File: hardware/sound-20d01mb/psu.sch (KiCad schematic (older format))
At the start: 26 parts

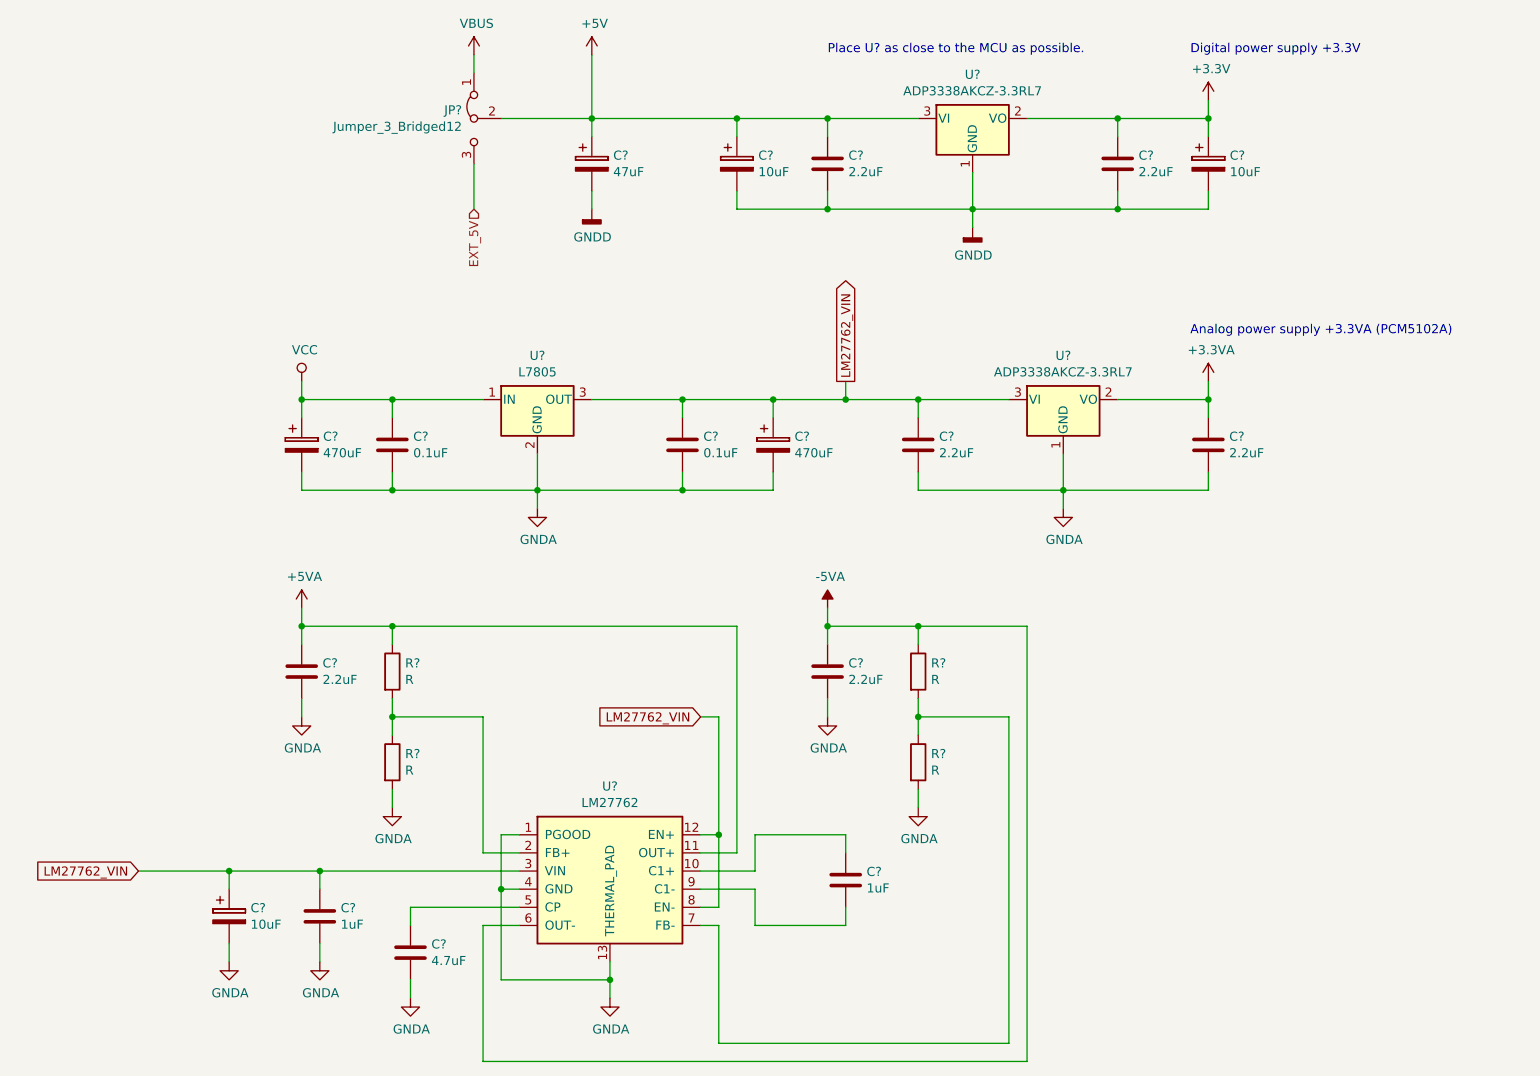
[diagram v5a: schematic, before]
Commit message: Added AD1938
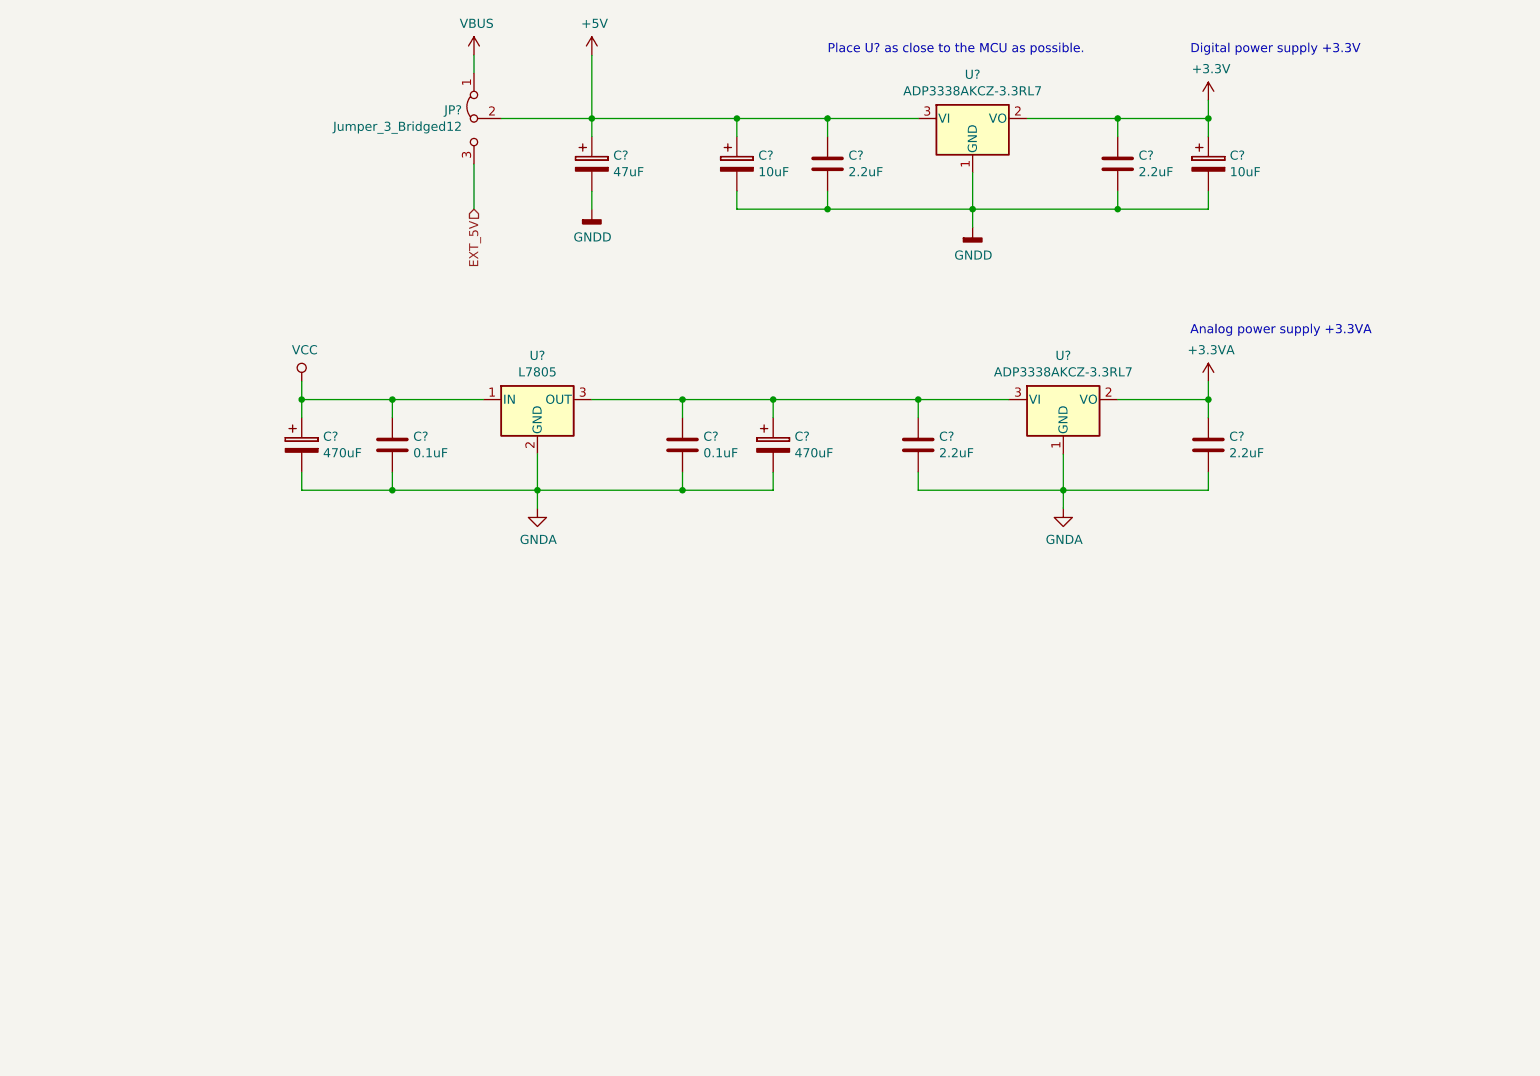
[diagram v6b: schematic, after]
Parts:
- removed C?: 4.7uF, Capacitor_SMD:C_1206_3216Metric_Pad1.42x1.75mm_HandSolder, symbol Device:C
- removed C? (x2): 1uF, Capacitor_SMD:C_1206_3216Metric_Pad1.42x1.75mm_HandSolder, symbol Device:C
- removed C? (x2): 2.2uF, Capacitor_SMD:C_1206_3216Metric_Pad1.42x1.75mm_HandSolder, symbol Device:C
- removed C?: 10uF, symbol Device:CP
- removed R? (x4): R, Resistor_SMD:R_1206_3216Metric_Pad1.42x1.75mm_HandSolder, symbol Device:R
- removed U?: LM27762, Package_SON:WSON-12-1EP_3x2mm_P0.5mm_EP1x2.65_ThermalVias, symbol sound-20d01_Library:LM27762
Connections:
- net LM27762_VIN: no longer names the net of C?.1, C?.1, C?.1, U?.3 (OUT), U?.3 (VI)
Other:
- note added: "Analog power supply +3.3VA"
- note removed: "Analog power supply +3.3VA (PCM5102A)"

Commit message: Updated schematics
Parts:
- removed C? (x2): 470uF, symbol Device:CP
- removed C? (x2): 0.1uF, Capacitor_SMD:C_1206_3216Metric_Pad1.42x1.75mm_HandSolder, symbol Device:C
- removed U?: L7805, symbol Regulator_Linear:L7805
- added C?: 10uF, symbol Device:CP
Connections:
- net +5V: now also C?.1, U?.3 (VI), C?.1
- net GNDA: now also C?.2
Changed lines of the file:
@@
 	1    0    0    -1
 $EndComp
-Connection ~ 5650 3300
 $Comp
 L power:VBUS #PWR?
@@
 Place U? as close to the MCU as possible.
 $Comp
-L Regulator_Linear:L7805 U?
-U 1 1 60EFE20B
-P 3550 3300
-F 0 "U?" H 3550 3542 50  0000 C CNN
-F 1 "L7805" H 3550 3451 50  0000 C CNN
-F 2 "" H 3575 3150 50  0001 L CIN
-F 3 "http://www.st.com/content/ccc/resource/technical/document/datasheet/41/4f/b3/b0/12/d4/47/88/CD00000444.pdf/files/CD00000444.pdf/jcr:content/translations/en.CD00000444.pdf" H 3550 3250 50  0001 C CNN
-	1    3550 3300
-	1    0    0    -1
-$EndComp
-$Comp
-L power:VCC #PWR?
-U 1 1 60EFE34E
-P 2250 3200
-F 0 "#PWR?" H 2250 3050 50  0001 C CNN
-F 1 "VCC" H 2267 3373 50  0000 C CNN
-F 2 "" H 2250 3200 50  0001 C CNN
-F 3 "" H 2250 3200 50  0001 C CNN
-	1    2250 3200
-	1    0    0    -1
-$EndComp
-$Comp
-L Device:CP C?
-U 1 1 60EFECE5
-P 2250 3550
-F 0 "C?" H 2368 3596 50  0000 L CNN
-F 1 "470uF" H 2368 3505 50  0000 L CNN
-F 2 "" H 2288 3400 50  0001 C CNN
-F 3 "~" H 2250 3550 50  0001 C CNN
-	1    2250 3550
-	1    0    0    -1
-$EndComp
-$Comp
-L Device:C C?
-U 1 1 60EFED6F
-P 2750 3550
-AR Path="/60DE2DF4/60EFED6F" Ref="C?"  Part="1"
-AR Path="/60DE2DF1/60EFED6F" Ref="C?"  Part="1"
-AR Path="/61033008/60EFED6F" Ref="C?"  Part="1"
-F 0 "C?" H 2865 3596 50  0000 L CNN
-F 1 "0.1uF" H 2865 3505 50  0000 L CNN
-F 2 "Capacitor_SMD:C_1206_3216Metric_Pad1.42x1.75mm_HandSolder" H 2788 3400 50  0001 C CNN
-F 3 "~" H 2750 3550 50  0001 C CNN
-	1    2750 3550
+L power:+5V #PWR?
+U 1 1 613DA71E
+P 5150 3200
+F 0 "#PWR?" H 5150 3050 50  0001 C CNN
+F 1 "+5V" H 5165 3373 50  0000 C CNN
+F 2 "" H 5150 3200 50  0001 C CNN
+F 3 "" H 5150 3200 50  0001 C CNN
+	1    5150 3200
 	1    0    0    -1
 $EndComp
 Wire Wire Line
-	2250 3300 2750 3300
-Wire Wire Line
-	2250 3300 2250 3400
-Wire Wire Line
-	2750 3400 2750 3300
-Wire Wire Line
-	2750 3300 3250 3300
-Connection ~ 2750 3300
-Wire Wire Line
-	2250 3200 2250 3300
-Connection ~ 2250 3300
-Wire Wire Line
-	3850 3300 4350 3300
+	5150 3300 5150 3200
+Connection ~ 5650 3300
 $Comp
-L Device:C C?
-U 1 1 60F07D83
-P 4350 3550
-AR Path="/60DE2DF4/60F07D83" Ref="C?"  Part="1"
-AR Path="/60DE2DF1/60F07D83" Ref="C?"  Part="1"
-AR Path="/61033008/60F07D83" Ref="C?"  Part="1"
-F 0 "C?" H 4465 3596 50  0000 L CNN
-F 1 "0.1uF" H 4465 3505 50  0000 L CNN
-F 2 "Capacitor_SMD:C_1206_3216Metric_Pad1.42x1.75mm_HandSolder" H 4388 3400 50  0001 C CNN
-F 3 "~" H 4350 3550 50  0001 C CNN
-	1    4350 3550
+L Device:CP C?
+U 1 1 613DBAC3
+P 5150 3550
+F 0 "C?" H 5268 3596 50  0000 L CNN
+F 1 "10uF" H 5268 3505 50  0000 L CNN
+F 2 "" H 5188 3400 50  0001 C CNN
+F 3 "~" H 5150 3550 50  0001 C CNN
+	1    5150 3550
 	1    0    0    -1
 $EndComp
 Wire Wire Line
-	4350 3400 4350 3300
-$Comp
-L Device:CP C?
-U 1 1 60F08839
-P 4850 3550
-F 0 "C?" H 4968 3596 50  0000 L CNN
-F 1 "470uF" H 4968 3505 50  0000 L CNN
-F 2 "" H 4888 3400 50  0001 C CNN
-F 3 "~" H 4850 3550 50  0001 C CNN
-	1    4850 3550
-	1    0    0    -1
-$EndComp
+	5150 3300 5650 3300
 Wire Wire Line
-	4350 3300 4850 3300
-Connection ~ 4350 3300
+	5150 3300 5150 3400
+Connection ~ 5150 3300
 Wire Wire Line
-	4850 3400 4850 3300
-Connection ~ 4850 3300
-$Comp
-L power:GNDA #PWR?
-U 1 1 60F0C362
-P 3550 3900
-F 0 "#PWR?" H 3550 3650 50  0001 C CNN
-F 1 "GNDA" H 3555 3727 50  0000 C CNN
-F 2 "" H 3550 3900 50  0001 C CNN
-F 3 "" H 3550 3900 50  0001 C CNN
-	1    3550 3900
-	1    0    0    -1
-$EndComp
+	5150 3700 5150 3800
 Wire Wire Line
-	3550 3600 3550 3800
-Wire Wire Line
-	2250 3700 2250 3800
-Wire Wire Line
-	2250 3800 2750 3800
-Connection ~ 3550 3800
-Wire Wire Line
-	3550 3800 3550 3900
-Wire Wire Line
-	2750 3700 2750 3800
-Connection ~ 2750 3800
-Wire Wire Line
-	2750 3800 3550 3800
-Wire Wire Line
-	4350 3700 4350 3800
-Wire Wire Line
-	4350 3800 3550 3800
-Wire Wire Line
-	4850 3700 4850 3800
-Wire Wire Line
-	4850 3800 4350 3800
-Connection ~ 4350 3800
-Wire Wire Line
-	4850 3300 5650 3300
+	5150 3800 5650 3800
+Connection ~ 5650 3800
 $EndSCHEMATC

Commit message: Updated PSU and DAC
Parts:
- added D?: LED, LED_SMD:LED_1206_3216Metric_Pad1.42x1.75mm_HandSolder, symbol Device:LED
- added R?: R, Resistor_SMD:R_1206_3216Metric_Pad1.42x1.75mm_HandSolder, symbol Device:R
- C? (x3): footprint (none) -> Capacitor_SMD:CP_Elec_4x5.4
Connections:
- wire segments 42 -> 45
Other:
- note added: "Analog power supply (DAC)"
- note added: "Digital power supply"
- note added: "Place U? as close\nto the DAC as possible."
- note added: "Place U? as close\nto the MCU as possible."
- note removed: "Analog power supply +3.3VA"
- note removed: "Digital power supply +3.3V"
- note removed: "Place U? as close to the MCU as possible."
- moved on the sheet: C?, JP?, U?
